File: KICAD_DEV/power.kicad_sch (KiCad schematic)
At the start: 22 parts, among them J1 USB_C_Receptacle_USB2.0_14P, J2 Screw_Terminal_01x02, U2 USBLC6-2SC6, U3 LMR33640ADDA, U4 LM1086S-3.3/TR

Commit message: heading to school!
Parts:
- added C16: 100uF, Capacitor_SMD:C_Elec_10x10.2, symbol Device:C
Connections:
- net +12V: now also C16.1
- net GND: now also C16.2
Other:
- moved on the sheet: C1, C11, C12, C13, C14, C15, C2, C3, C4, C5, C6, F1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

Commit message: grounding and working on power, added the 100uF cap
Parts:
- C16: footprint Capacitor_SMD:C_Elec_10x10.2 -> Capacitor_SMD:C_Elec_6.3x5.8; Part RVT1E101M0607 -> MA25V100M6x6
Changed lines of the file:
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@@
 			)
 		)
-		(property "Footprint" "Capacitor_SMD:C_Elec_10x10.2"
+		(property "Footprint" "Capacitor_SMD:C_Elec_6.3x5.8"
 			(at 73.3552 77.47 0)
 			(effects
@@
 			)
 		)
-		(property "Part" "RVT1E101M0607"
+		(property "Part" "MA25V100M6x6"
 			(at 84.074 75.946 0)
 			(effects

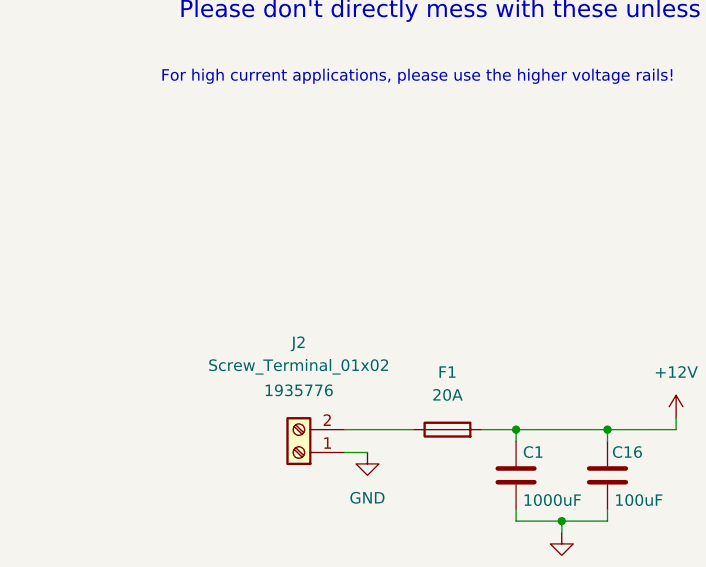
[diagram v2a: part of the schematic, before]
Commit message: finished routing the power!
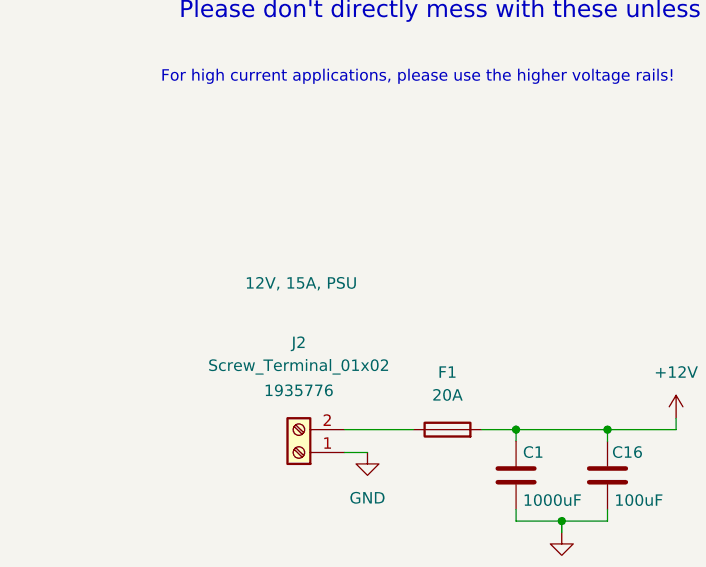
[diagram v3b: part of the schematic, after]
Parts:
- J2: Power (none) -> 12V, 15A, PSU
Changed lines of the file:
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@@
+			)
+		)
+		(property "Power" "12V, 15A, PSU"
+			(at 38.354 52.324 0)
+			(effects
+				(font
+					(size 1.27 1.27)
+				)
 			)
 		)

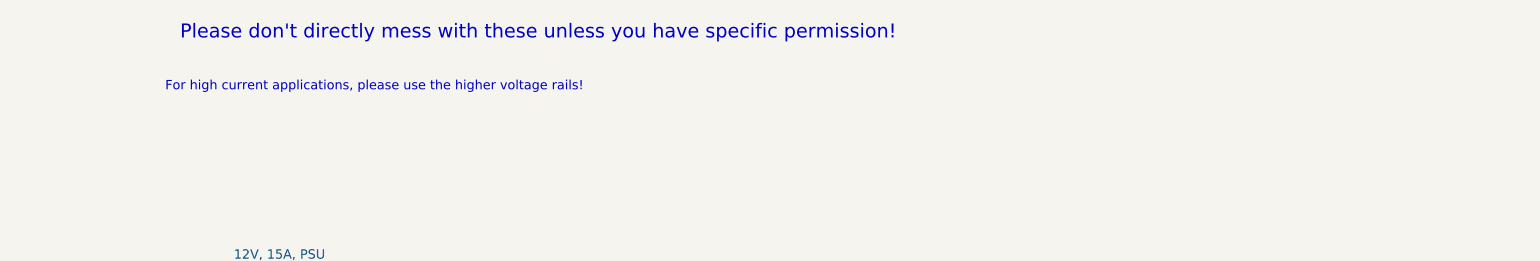
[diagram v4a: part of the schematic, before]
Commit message: wired the TMC2209 to my MCU, also more instructions on the schematic!
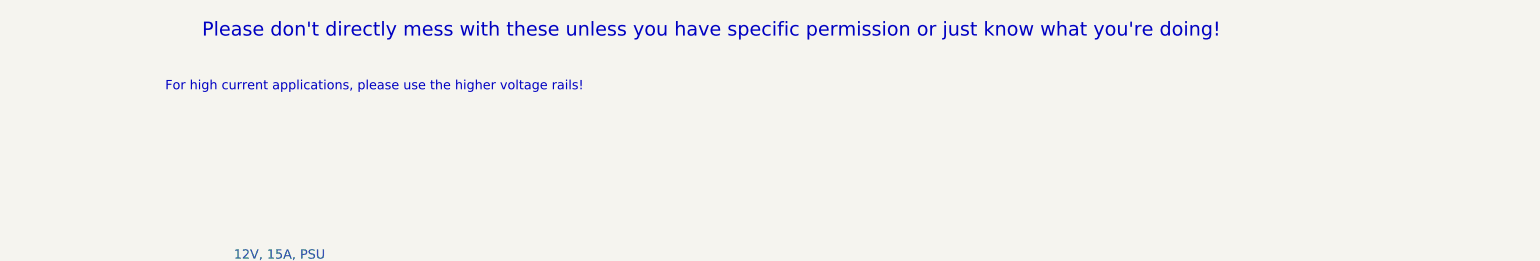
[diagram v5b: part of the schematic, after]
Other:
- note added: "Please don't directly mess with these unless you have specific permission or just know what you're doing!"
- note removed: "Please don't directly mess with these unless you have specific permission!"
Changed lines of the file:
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@@
 	(generator_version "9.0")
 	(paper "A4")
-	(text "Please don't directly mess with these unless you have specific permission!"
+	(text "Please don't directly mess with these unless you have specific permission or just know what you're doing!"
 		(exclude_from_sim no)
-		(at 73.66 22.098 0)
+		(at 97.282 21.844 0)
 		(effects
 			(font
